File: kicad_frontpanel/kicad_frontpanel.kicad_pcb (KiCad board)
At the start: 2 copper layers, 30 x 128.5 mm, 9 parts

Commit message: feat: :bookmark: rev 0.2 frontpanel
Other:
- board text added: "rev 0.2"
- board text removed: "rev 0.1"
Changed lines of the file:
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@@
   (gr_line locked (start 32.078299 74.690318) (end 32.104292 74.83589)
     (stroke (width 0.1) (type solid)) (layer "User.8"))
-  (gr_text "rev 0.1" (at 30 137) (layer "B.SilkS")
+  (gr_text "rev 0.2" (at 30 137) (layer "B.SilkS")
     (effects (font (size 0.8 0.8) (thickness 0.1) bold) (justify left bottom mirror))
   )

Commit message: feat: :lipstick: update design files, overall design system, clean placement file
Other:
- board text added: "rev 0.2 l-i-l.de"
- board text removed: "rev 0.2"

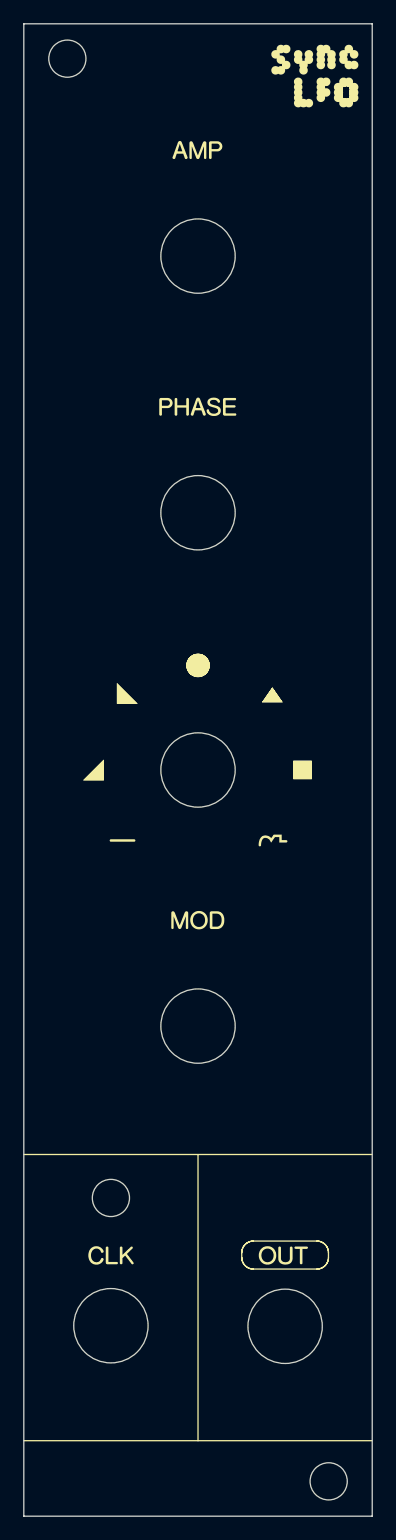
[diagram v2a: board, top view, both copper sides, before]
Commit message: feat: :sparkles: inv output, new design, reposition
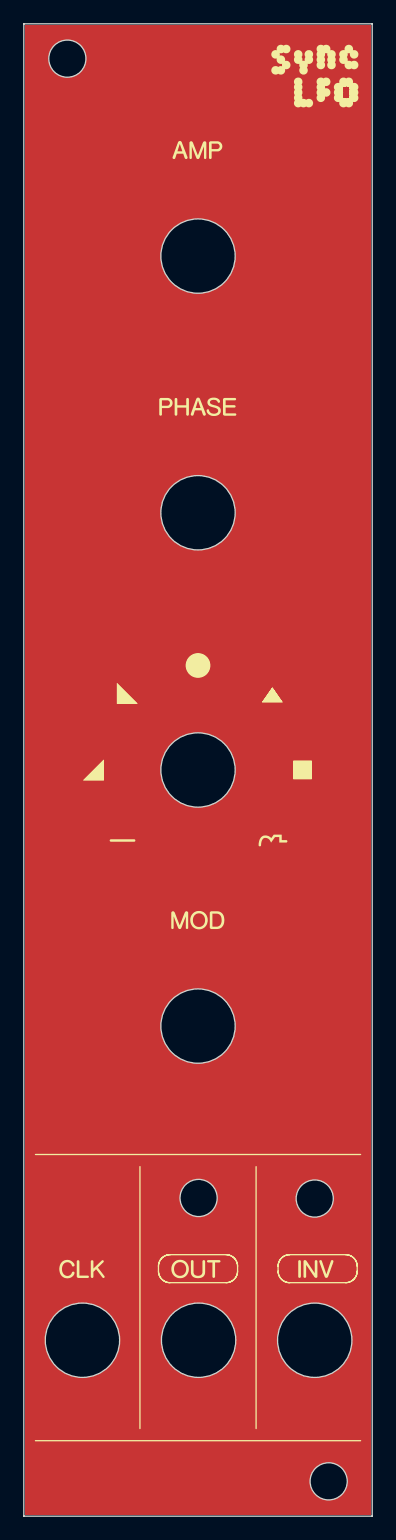
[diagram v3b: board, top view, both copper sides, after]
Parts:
- added REF**: MountingHole_6.4mm_M6, MountingHole:MountingHole_6.4mm_M6, F.Cu at (25.1, 123.3)
- added locked: MountingHole_3.2mm_M3, MountingHole:MountingHole_3.2mm_M3, F.Cu at (45.0, 111.2)
- moved REF** 7.65 mm to (35.0, 123.3)
- moved locked 7.55 mm to (35.0, 111.1)
- moved REF** 2.82 mm to (45.0, 123.3)
